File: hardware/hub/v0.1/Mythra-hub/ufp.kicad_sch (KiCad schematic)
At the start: 12 parts, among them J1 918-418K2022C40000, U2 HD3SS460

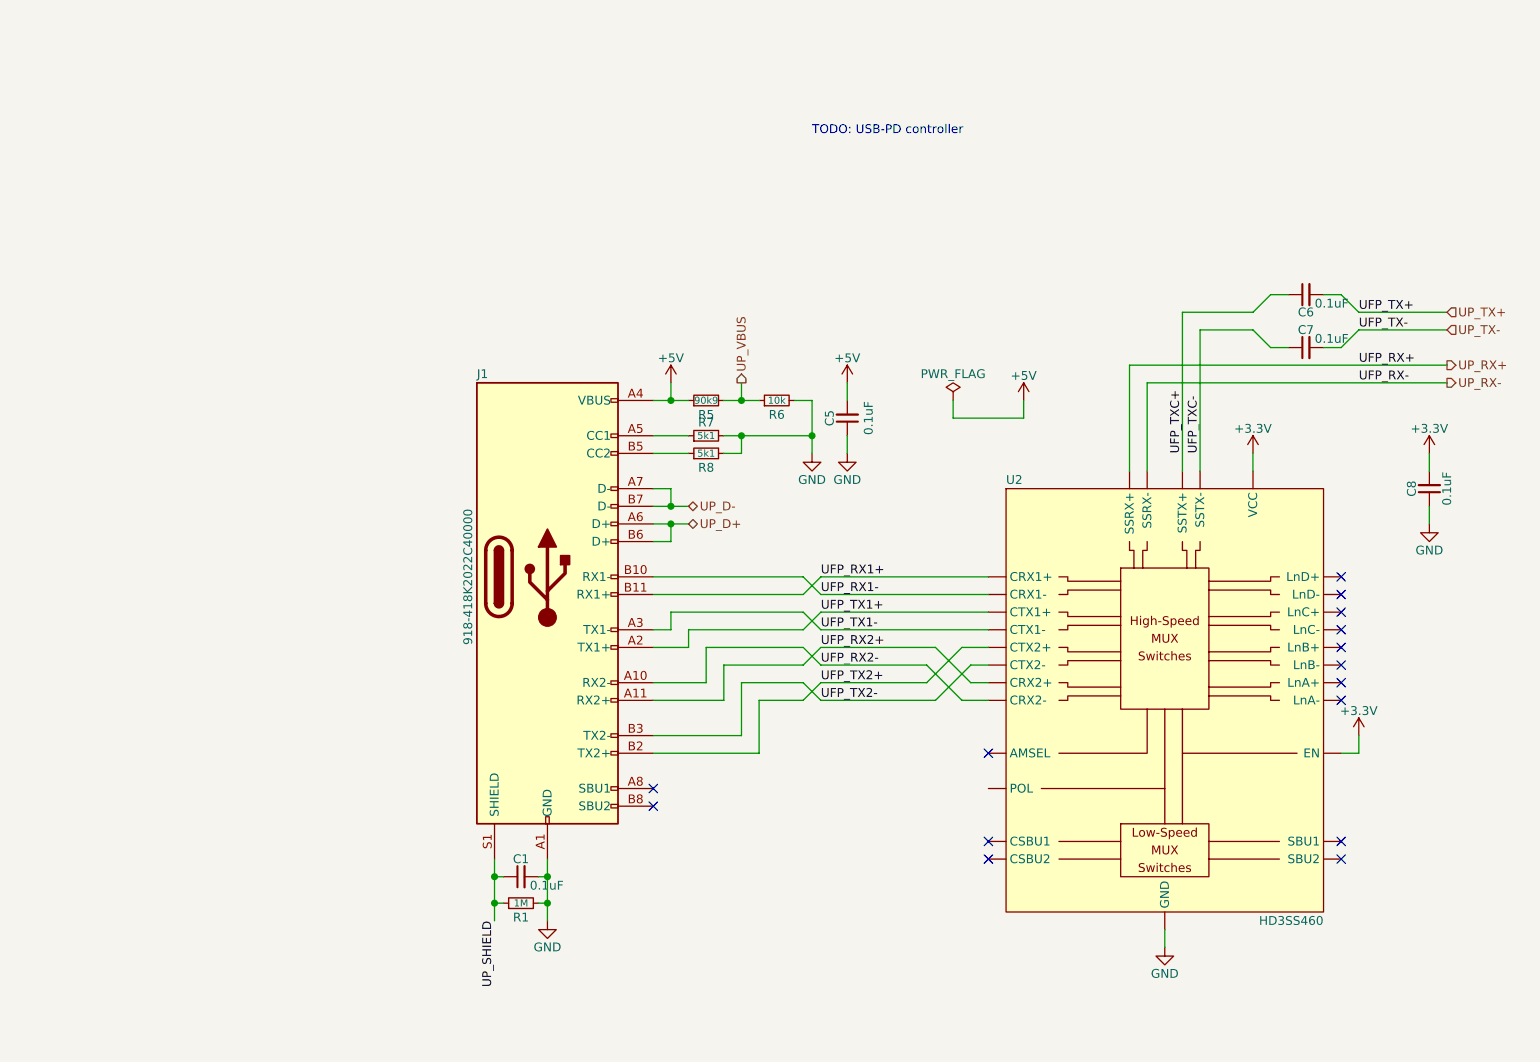
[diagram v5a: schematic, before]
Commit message: Version controlled the changes from the last stream, including the addition of the 3.3V DC-DC, config I2C EEPROM and test points
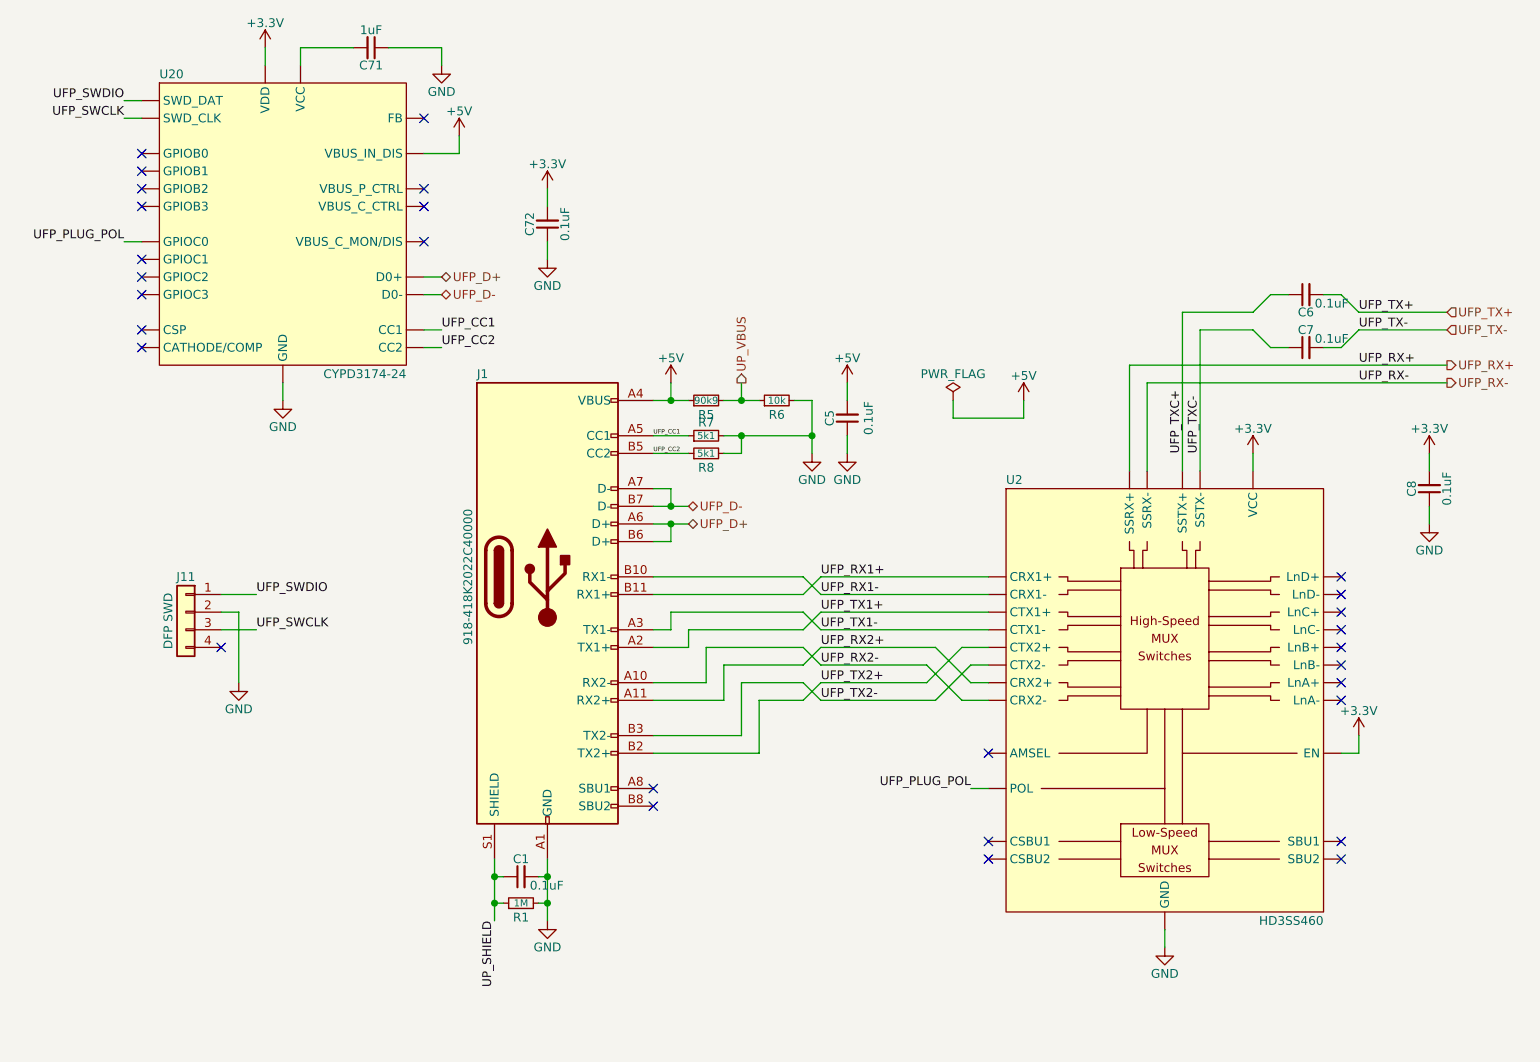
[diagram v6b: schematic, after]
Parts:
- added C71: 1uF, rhais_rcl:C0402, symbol Device:C_Small
- added C72: 0.1uF, rhais_rcl:C0402, symbol Device:C_Small
- added J11: DFP SWD, rhais_connector-pinheader:PinHeader_1x04_P1.27mm_Vertical, symbol Connector_Generic:Conn_01x04
- added U20: CYPD3174-24, rhais_package-qfn:QFN-24-1EP_4x4mm_P0.5mm_EP2.6x2.6mm, symbol DX-MON:CYPD3174-24
- C1, C5, C6, C7, C8: MFR (none) -> Yageo; MPN (none) -> RC0402FR-0710KL; OC_LCSC (none) -> C60490; URL_LCSC (none) -> https://www.lcsc.com/product-detail/Chip-Resistor-Surface-M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
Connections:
- net +3V3: now also C72.2, U20.23 (VDD)
- net +5V: now also U20.18 (VBUS_IN_DIS)
- net GND: now also C71.1, C72.1, J11.2 (Pin_2), U20.15 (GND), U20.25 (GND)
- net UFP_CC1: now reaches J1.A5 (CC1), R7.1
- net UFP_CC1: now also U20.15 (GND)
- net UFP_CC2: now reaches J1.B5 (CC2), R8.1
- net UFP_CC2: now also U20.14 (CC2)
- net UFP_PLUG_POL: now reaches U2.3 (POL)
- net UFP_PLUG_POL: now also U20.9 (GPIOC0)
- net UP_D+ renamed UFP_D+
- net UFP_D+: now also U20.17 (GPIOD0)
- net UP_D- renamed UFP_D-
- net UFP_D-: now also U20.16 (GPIOD1)
- net UP_RX+ renamed UFP_RX+
- net UP_RX- renamed UFP_RX-
- net UP_TX+ renamed UFP_TX+
- net UP_TX- renamed UFP_TX-
- new net: C71.2, U20.24 (VCC)
- new net UFP_SWCLK: J11.3 (Pin_3), U20.8 (GPIOA1)
- new net UFP_SWDIO: J11.1 (Pin_1), U20.7 (GPIOA0)
- no-connect marks 15 -> 29
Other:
- note removed: "TODO: USB-PD controller"

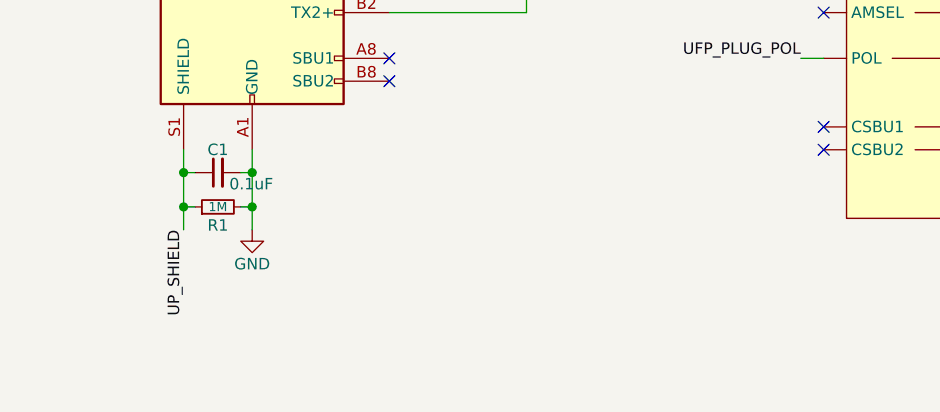
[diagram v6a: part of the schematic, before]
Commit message: Completed a first pass on the azonenburg schematic checklist and begun adding the per-port indicator LEDs that had been forgotten
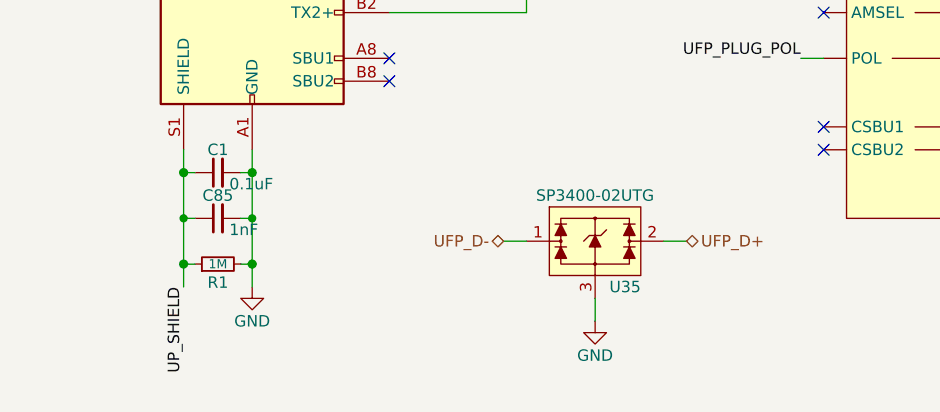
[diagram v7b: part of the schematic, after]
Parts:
- added C85: 1nF, rhais_rcl:C0402, symbol Device:C_Small
- added U35: SP3400-02UTG, rhais_package-qfn:UDFN-6L, symbol DX-MON:SP3400-02UTG
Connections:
- net GND: now also C85.2, U35.3 (GND), U35.4 (GND)
- net UFP_D+: now also U35.2 (IO2), U35.5 (NC)
- net UFP_D-: now also U35.1 (IO1), U35.6 (NC)
- net UP_SHIELD: now also C85.1
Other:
- moved on the sheet: R1
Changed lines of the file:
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@@
   (paper "A4")
   (junction (at 81.28 144.78) (diameter 1.016) (color 0 0 0 0))
-  (junction (at 81.28 148.59) (diameter 1.016) (color 0 0 0 0))
+  (junction (at 81.28 149.86) (diameter 0) (color 0 0 0 0))
+  (junction (at 81.28 154.94) (diameter 1.016) (color 0 0 0 0))
   (junction (at 88.9 144.78) (diameter 1.016) (color 0 0 0 0))
-  (junction (at 88.9 148.59) (diameter 1.016) (color 0 0 0 0))
+  (junction (at 88.9 149.86) (diameter 0) (color 0 0 0 0))
+  (junction (at 88.9 154.94) (diameter 1.016) (color 0 0 0 0))
   (junction (at 106.68 76.2) (diameter 1.016) (color 0 0 0 0))
   (junction (at 106.68 91.44) (diameter 1.016) (color 0 0 0 0))
@@
     (stroke (width 0) (type solid) (color 0 0 0 0))
   )
-  (wire (pts (xy 81.28 148.59) (xy 81.28 144.78))
-    (stroke (width 0) (type solid) (color 0 0 0 0))
-  )
-  (wire (pts (xy 81.28 148.59) (xy 81.28 151.13))
+  (wire (pts (xy 81.28 144.78) (xy 81.28 149.86))
+    (stroke (width 0) (type solid) (color 0 0 0 0))
+  )
+  (wire (pts (xy 81.28 149.86) (xy 81.28 154.94))
+    (stroke (width 0) (type solid) (color 0 0 0 0))
+  )
+  (wire (pts (xy 81.28 154.94) (xy 81.28 157.48))
     (stroke (width 0) (type solid) (color 0 0 0 0))
   )
@@
     (stroke (width 0) (type solid) (color 0 0 0 0))
   )
-  (wire (pts (xy 82.55 148.59) (xy 81.28 148.59))
+  (wire (pts (xy 82.55 149.86) (xy 81.28 149.86))
+    (stroke (width 0) (type default) (color 0 0 0 0))
+  )
+  (wire (pts (xy 82.55 154.94) (xy 81.28 154.94))
     (stroke (width 0) (type solid) (color 0 0 0 0))
   )
@@
     (stroke (width 0) (type solid) (color 0 0 0 0))
   )
-  (wire (pts (xy 87.63 148.59) (xy 88.9 148.59))
+  (wire (pts (xy 87.63 149.86) (xy 88.9 149.86))
+    (stroke (width 0) (type default) (color 0 0 0 0))
+  )
+  (wire (pts (xy 87.63 154.94) (xy 88.9 154.94))
     (stroke (width 0) (type solid) (color 0 0 0 0))
   )
@@
     (stroke (width 0) (type solid) (color 0 0 0 0))
   )
-  (wire (pts (xy 88.9 148.59) (xy 88.9 144.78))
-    (stroke (width 0) (type solid) (color 0 0 0 0))
-  )
-  (wire (pts (xy 88.9 151.13) (xy 88.9 148.59))
+  (wire (pts (xy 88.9 144.78) (xy 88.9 149.86))
+    (stroke (width 0) (type solid) (color 0 0 0 0))
+  )
+  (wire (pts (xy 88.9 149.86) (xy 88.9 154.94))
+    (stroke (width 0) (type solid) (color 0 0 0 0))
+  )
+  (wire (pts (xy 88.9 157.48) (xy 88.9 154.94))
     (stroke (width 0) (type solid) (color 0 0 0 0))
   )
@@
     (stroke (width 0) (type solid) (color 0 0 0 0))
   )
+  (wire (pts (xy 116.84 152.4) (xy 119.38 152.4))
+    (stroke (width 0) (type solid) (color 0 0 0 0))
+  )
   (wire (pts (xy 119.38 76.2) (xy 116.84 76.2))
     (stroke (width 0) (type solid) (color 0 0 0 0))
@@
     (stroke (width 0) (type solid) (color 0 0 0 0))
   )
+  (wire (pts (xy 127 161.29) (xy 127 158.75))
+    (stroke (width 0) (type default) (color 0 0 0 0))
+  )
   (wire (pts (xy 128.27 101.6) (xy 125.73 104.14))
     (stroke (width 0) (type solid) (color 0 0 0 0))
@@
   )
   (wire (pts (xy 132.08 81.28) (xy 132.08 83.82))
+    (stroke (width 0) (type solid) (color 0 0 0 0))
+  )
+  (wire (pts (xy 137.16 152.4) (xy 134.62 152.4))
     (stroke (width 0) (type solid) (color 0 0 0 0))
   )
@@
     (effects (font (size 1.27 1.27)) (justify left bottom))
   )
-  (label "UP_SHIELD" (at 81.28 151.13 270)
+  (label "UP_SHIELD" (at 81.28 157.48 270)
     (effects (font (size 1.27 1.27)) (justify right bottom))
   )
@@
     (effects (font (size 1.27 1.27)) (justify left))
   )
+  (hierarchical_label "UFP_D-" (shape bidirectional) (at 116.84 152.4 180)
+    (effects (font (size 1.27 1.27)) (justify right))
+  )
+  (hierarchical_label "UFP_D+" (shape bidirectional) (at 137.16 152.4 0)
+    (effects (font (size 1.27 1.27)) (justify left))
+  )
   (hierarchical_label "UFP_TX+" (shape input) (at 218.44 63.5 0)
     (effects (font (size 1.27 1.27)) (justify left))
@@
     (pin "1")
   )
-  (symbol (lib_id "power:GND") (at 88.9 151.13 0) (unit 1)
-    (in_bom yes) (on_board yes)
-    (property "Reference" "#PWR06" (id 0) (at 88.9 157.48 0)
-      (effects (font (size 1.27 1.27)) hide)
-    )
-    (property "Value" "GND" (id 1) (at 88.9 154.94 0))
-    (property "Footprint" "" (id 2) (at 88.9 151.13 0)
-      (effects (font (size 1.27 1.27)) hide)
-    )
-    (property "Datasheet" "" (id 3) (at 88.9 151.13 0)
+  (symbol (lib_id "power:GND") (at 88.9 157.48 0) (unit 1)
+    (in_bom yes) (on_board yes)
+    (property "Reference" "#PWR06" (id 0) (at 88.9 163.83 0)
+      (effects (font (size 1.27 1.27)) hide)
+    )
+    (property "Value" "GND" (id 1) (at 88.9 161.29 0))
+    (property "Footprint" "" (id 2) (at 88.9 157.48 0)
+      (effects (font (size 1.27 1.27)) hide)
+    )
+    (property "Datasheet" "" (id 3) (at 88.9 157.48 0)
       (effects (font (size 1.27 1.27)) hide)
     )
@@
     (pin "1")
   )
+  (symbol (lib_id "power:GND") (at 127 161.29 0) (unit 1)
+    (in_bom yes) (on_board yes)
+    (property "Reference" "#PWR0169" (id 0) (at 127 167.64 0)
+      (effects (font (size 1.27 1.27)) hide)
+    )
+    (property "Value" "GND" (id 1) (at 127 165.1 0))
+    (property "Footprint" "" (id 2) (at 127 161.29 0)
+      (effects (font (size 1.27 1.27)) hide)
+    )
+    (property "Datasheet" "" (id 3) (at 127 161.29 0)
+      (effects (font (size 1.27 1.27)) hide)
+    )
+    (pin "1")
+  )
   (symbol (lib_id "power:GND") (at 132.08 83.82 0) (unit 1)
     (in_bom yes) (on_board yes)
@@
     (pin "1")
   )
-  (symbol (lib_id "Device:R_Small") (at 85.09 148.59 90) (unit 1)
-    (in_bom yes) (on_board yes)
-    (property "Reference" "R1" (id 0) (at 85.09 151.384 90)
+  (symbol (lib_id "Device:R_Small") (at 85.09 154.94 90) (unit 1)
+    (in_bom yes) (on_board yes)
+    (property "Reference" "R1" (id 0) (at 85.09 157.734 90)
       (effects (font (size 1.27 1.27)) (justify top))
     )
-    (property "Value" "1M" (id 1) (at 85.09 148.59 90)
+    (property "Value" "1M" (id 1) (at 85.09 154.94 90)
       (effects (font (size 1.016 1.016)))
     )
-    (property "Footprint" "rhais_rcl:R0402" (id 2) (at 85.09 148.59 0)
-      (effects (font (size 1.27 1.27)) hide)
-    )
-    (property "Datasheet" "https://www.farnell.com/datasheets/2860681.pdf" (id 3) (at 85.09 148.59 0)
-      (effects (font (size 1.27 1.27)) hide)
-    )
-    (property "MFR" "Multicomp Pro" (id 4) (at 85.09 148.59 0)
-      (effects (font (size 1.27 1.27)) hide)
-    )
-    (property "MPN" "MCWR04X1004FTL" (id 5) (at 85.09 148.59 0)
-      (effects (font (size 1.27 1.27)) hide)
-    )
-    (property "OC_FARNELL" "2447127" (id 6) (at 85.09 148.59 0)
-      (effects (font (size 1.27 1.27)) hide)
-    )
-    (property "URL_FARNELL" "https://uk.farnell.com/multicomp/mcwr04x1004ftl/res-1m-1-0-0625w-0402-thick-film/dp/2447127" (id 7) (at 85.09 148.59 0)
+    (property "Footprint" "rhais_rcl:R0402" (id 2) (at 85.09 154.94 0)
+      (effects (font (size 1.27 1.27)) hide)
+    )
+    (property "Datasheet" "https://www.farnell.com/datasheets/2860681.pdf" (id 3) (at 85.09 154.94 0)
+      (effects (font (size 1.27 1.27)) hide)
+    )
+    (property "MFR" "Multicomp Pro" (id 4) (at 85.09 154.94 0)
+      (effects (font (size 1.27 1.27)) hide)
+    )
+    (property "MPN" "MCWR04X1004FTL" (id 5) (at 85.09 154.94 0)
+      (effects (font (size 1.27 1.27)) hide)
+    )
+    (property "OC_FARNELL" "2447127" (id 6) (at 85.09 154.94 0)
+      (effects (font (size 1.27 1.27)) hide)
+    )
+    (property "URL_FARNELL" "https://uk.farnell.com/multicomp/mcwr04x1004ftl/res-1m-1-0-0625w-0402-thick-film/dp/2447127" (id 7) (at 85.09 154.94 0)
       (effects (font (size 1.27 1.27)) hide)
     )
@@
     (pin "2")
   )
+  (symbol (lib_id "Device:C_Small") (at 85.09 149.86 90) (unit 1)
+    (in_bom yes) (on_board yes)
+    (property "Reference" "C85" (id 0) (at 85.09 147.32 90))
+    (property "Value" "1nF" (id 1) (at 86.36 151.13 90)
+      (effects (font (size 1.27 1.27)) (justify right))
+    )
+    (property "Footprint" "rhais_rcl:C0402" (id 2) (at 85.09 149.86 0)
+      (effects (font (size 1.27 1.27)) hide)
+    )
+    (property "Datasheet" "https://www.yageo.com/upload/media/product/productsearch/datasheet/rchip/PYu-RC_Group_51_RoHS_L_11.pdf" (id 3) (at 85.09 149.86 0)
+      (effects (font (size 1.27 1.27)) hide)
+    )
+    (property "MFR" "Yageo" (id 4) (at 85.09 149.86 0)
+      (effects (font (size 1.27 1.27)) hide)
+    )
+    (property "MPN" "RC0402FR-0710KL" (id 5) (at 85.09 149.86 0)
+      (effects (font (size 1.27 1.27)) hide)
+    )
+    (property "OC_LCSC" "C60490" (id 6) (at 85.09 149.86 0)
+      (effects (font (size 1.27 1.27)) hide)
+    )
+    (property "URL_LCSC" "https://www.lcsc.com/product-detail/Chip-Resistor-Surface-Mount_YAGEO-RC0402FR-0710KL_C60490.html" (id 7) (at 85.09 149.86 0)
+      (effects (font (size 1.27 1.27)) hide)
+    )
+    (pin "1")
+    (pin "2")
+  )
   (symbol (lib_id "Device:C_Small") (at 88.9 50.8 180) (unit 1)
     (in_bom yes) (on_board yes)
@@
     (pin "4")
   )
+  (symbol (lib_id "DX-MON:SP3400-02UTG") (at 127 152.4 0) (unit 1)
+    (in_bom yes) (on_board yes)
+    (property "Reference" "U35" (id 0) (at 132.08 157.48 0)
+      (effects (font (size 1.27 1.27)) (justify right))
+    )
+    (property "Value" "SP3400-02UTG" (id 1) (at 127 147.32 0))
+    (property "Footprint" "rhais_package-qfn:UDFN-6L" (id 2) (at 127 152.4 0)
+      (effects (font (size 1.27 1.27)) hide)
+    )
+    (property "Datasheet" "https://www.littelfuse.com/~/media/electronics/datasheets/tvs_diode_arrays/littelfuse_tvs_diode_array_sp3400_datasheet.pdf" (id 3) (at 127 171.45 0)
+      (effects (font (size 1.27 1.27)) hide)
+    )
+    (property "MFR" "Littlefuse" (id 4) (at 127 166.37 0)
+      (effects (font (size 1.27 1.27)) hide)
+    )
+    (property "MPN" "SP3400-02UTG" (id 5) (at 127 168.91 0)
+      (effects (font (size 1.27 1.27)) hide)
+    )
+    (pin "1")
+    (pin "2")
+    (pin "3")
+    (pin "4")
+    (pin "5")
+    (pin "6")
+  )
   (symbol (lib_id "Connector:USB_C_Receptacle") (at 88.9 101.6 0) (unit 1)
